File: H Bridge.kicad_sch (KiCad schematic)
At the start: 58 parts, among them J4 Conn_01x02_Socket, Q11 IRLZ44N, Q110 IRLZ44N, Q111 BC557, Q112 BC547, Q113 BC557, Q120 IRLZ44N, Q121 BC557, Q122 BC547, Q123 BC557, Q14 BC547, Q15 BC557, Q17 BC547, Q18 BC547, Q2 BC547, Q210 BC547, Q6 BC547, Q7 BC557, Q9 IRLZ44N, U110 4N35, U2 4N35, U6 4N35, U7 4N35

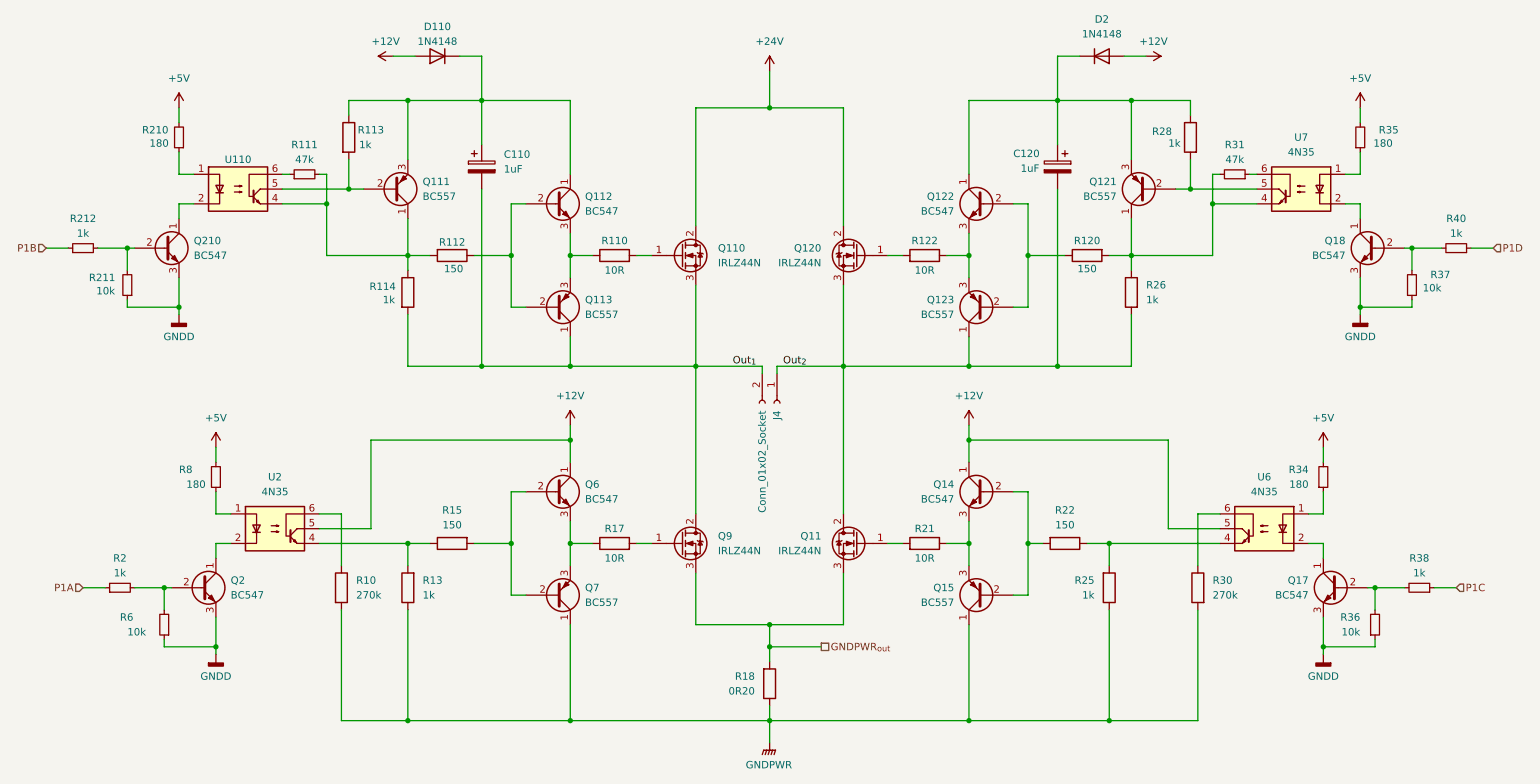
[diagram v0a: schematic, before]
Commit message: Placement H bridge & PSU
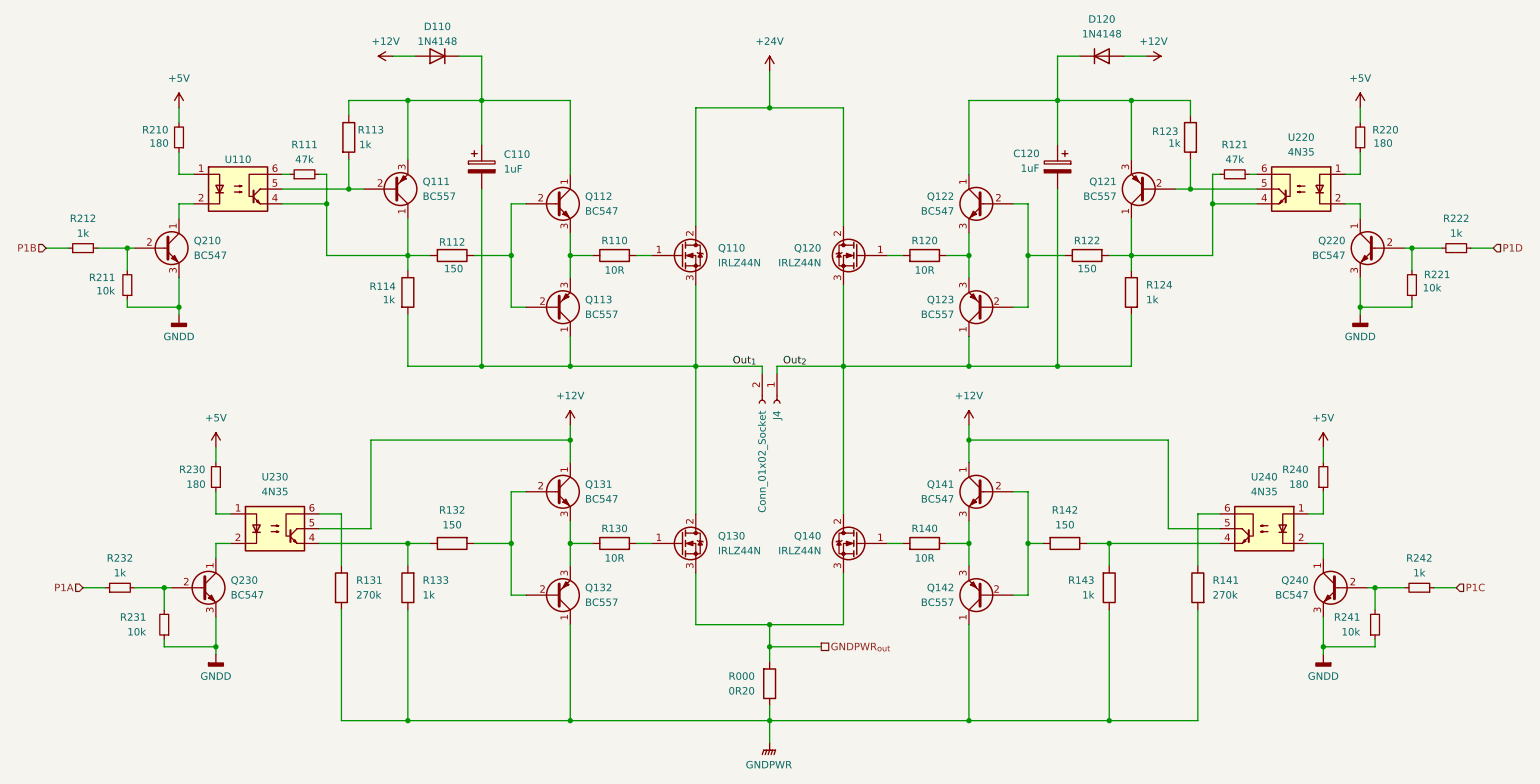
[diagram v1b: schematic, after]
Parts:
- renumbered D2 to D120, Q9 to Q130, Q6 to Q131, Q7 to Q132, Q11 to Q140, Q14 to Q141, Q15 to Q142, Q18 to Q220, Q2 to Q230, Q17 to Q240, R18 to R000, R122 to R120, R31 to R121, R120 to R122, R28 to R123, R26 to R124, R17 to R130, R10 to R131, R15 to R132, R13 to R133, R21 to R140, R30 to R141, R22 to R142, R25 to R143, R35 to R220, R37 to R221, R40 to R222, R8 to R230, R6 to R231, R2 to R232, R34 to R240, R36 to R241, R38 to R242, U7 to U220, U2 to U230, U6 to U240
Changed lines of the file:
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@@
 		(on_board yes)
 		(dnp no)
-		(property "Reference" "R122"
+		(property "Reference" "R120"
 			(at 175.26 64.77 90)
 			(effects
@@
 		(dnp no)
 		(fields_autoplaced yes)
-		(property "Reference" "R36"
+		(property "Reference" "R241"
 			(at 250.19 129.5399 0)
 			(effects
@@
 		(on_board yes)
 		(dnp no)
-		(property "Reference" "R2"
+		(property "Reference" "R232"
 			(at 36.83 119.38 90)
 			(effects
@@
 		(on_board yes)
 		(dnp no)
-		(property "Reference" "Q7"
+		(property "Reference" "Q132"
 			(at 116.84 124.4599 0)
 			(effects
@@
 		(dnp no)
 		(fields_autoplaced yes)
-		(property "Reference" "Q11"
+		(property "Reference" "Q140"
 			(at 157.48 115.5699 0)
 			(effects
@@
 		(dnp no)
 		(fields_autoplaced yes)
-		(property "Reference" "U7"
+		(property "Reference" "U220"
 			(at 240.03 46.99 0)
 			(effects
@@
 		(dnp no)
 		(fields_autoplaced yes)
-		(property "Reference" "R30"
+		(property "Reference" "R141"
 			(at 224.79 123.1899 0)
 			(effects
@@
 		(dnp no)
 		(fields_autoplaced yes)
-		(property "Reference" "Q14"
+		(property "Reference" "Q141"
 			(at 180.34 106.6799 0)
 			(effects
@@
 		(on_board yes)
 		(dnp no)
-		(property "Reference" "R8"
+		(property "Reference" "R230"
 			(at 46.99 104.14 0)
 			(effects
@@
 		(on_board yes)
 		(dnp no)
-		(property "Reference" "U2"
+		(property "Reference" "U230"
 			(at 63.5 105.41 0)
 			(effects
@@
 		(on_board yes)
 		(dnp no)
-		(property "Reference" "Q15"
+		(property "Reference" "Q142"
 			(at 180.34 124.4599 0)
 			(effects
@@
 		(dnp no)
 		(fields_autoplaced yes)
-		(property "Reference" "D2"
+		(property "Reference" "D120"
 			(at 205.74 26.67 0)
 			(effects
@@
 		(on_board yes)
 		(dnp no)
-		(property "Reference" "R6"
+		(property "Reference" "R231"
 			(at 36.83 129.54 0)
 			(effects
@@
 		(dnp no)
 		(fields_autoplaced yes)
-		(property "Reference" "R10"
+		(property "Reference" "R131"
 			(at 77.47 123.1899 0)
 			(effects
@@
 		(on_board yes)
 		(dnp no)
-		(property "Reference" "R34"
+		(property "Reference" "R240"
 			(at 241.3 104.1399 0)
 			(effects
@@
 		(dnp no)
 		(fields_autoplaced yes)
-		(property "Reference" "Q17"
+		(property "Reference" "Q240"
 			(at 241.3 123.1899 0)
 			(effects
@@
 		(dnp no)
 		(fields_autoplaced yes)
-		(property "Reference" "Q9"
+		(property "Reference" "Q130"
 			(at 139.7 115.5699 0)
 			(effects
@@
 		(on_board yes)
 		(dnp no)
-		(property "Reference" "R37"
+		(property "Reference" "R221"
 			(at 265.684 70.612 0)
 			(effects
@@
 		(on_board yes)
 		(dnp no)
-		(property "Reference" "R15"
+		(property "Reference" "R132"
 			(at 93.98 111.125 90)
 			(effects
@@
 		(dnp no)
 		(fields_autoplaced yes)
-		(property "Reference" "R18"
+		(property "Reference" "R000"
 			(at 146.05 139.6999 0)
 			(effects
@@
 			(project "Motor Control"
 				(path "/287fa568-d091-4161-b3b2-3036dfbfe9fa/78ba1051-b673-42a0-97cc-c42edd42c782"
-					(reference "R18")
+					(reference "R000")
 					(unit 1)
 				)
@@
 		(dnp no)
 		(fields_autoplaced yes)
-		(property "Reference" "Q18"
+		(property "Reference" "Q220"
 			(at 247.65 64.7699 0)
 			(effects
@@
 		(on_board yes)
 		(dnp no)
-		(property "Reference" "R35"
+		(property "Reference" "R220"
 			(at 256.794 45.72 0)
 			(effects
@@
 		(dnp no)
 		(fields_autoplaced yes)
-		(property "Reference" "R13"
+		(property "Reference" "R133"
 			(at 88.9 123.1899 0)
 			(effects
@@
 		(dnp no)
 		(fields_autoplaced yes)
-		(property "Reference" "R25"
+		(property "Reference" "R143"
 			(at 204.47 123.1899 0)
 			(effects
@@
 		(on_board yes)
 		(dnp no)
-		(property "Reference" "R26"
+		(property "Reference" "R124"
 			(at 213.36 72.3899 0)
 			(effects
@@
 		(on_board yes)
 		(dnp no)
-		(property "Reference" "R17"
+		(property "Reference" "R130"
 			(at 121.92 114.3 90)
 			(effects
@@
 		(dnp no)
 		(fields_autoplaced yes)
-		(property "Reference" "R38"
+		(property "Reference" "R242"
 			(at 260.35 119.38 90)
 			(effects
@@
 		(on_board yes)
 		(dnp no)
-		(property "Reference" "U6"
+		(property "Reference" "U240"
 			(at 233.68 105.41 0)
 			(effects
@@
 		(on_board yes)
 		(dnp no)
-		(property "Reference" "R28"
+		(property "Reference" "R123"
 			(at 214.376 45.974 0)
 			(effects
@@
 		(on_board yes)
 		(dnp no)
-		(property "Reference" "R22"
+		(property "Reference" "R142"
 			(at 199.39 111.125 90)
 			(effects
@@
 		(dnp no)
 		(fields_autoplaced yes)
-		(property "Reference" "Q6"
+		(property "Reference" "Q131"
 			(at 116.84 106.6799 0)
 			(effects
@@
 		(on_board yes)
 		(dnp no)
-		(property "Reference" "R21"
+		(property "Reference" "R140"
 			(at 175.26 114.3 90)
 			(effects
@@
 		(dnp no)
 		(fields_autoplaced yes)
-		(property "Reference" "Q2"
+		(property "Reference" "Q230"
 			(at 55.88 123.1899 0)
 			(effects
@@
 		(on_board yes)
 		(dnp no)
-		(property "Reference" "R31"
+		(property "Reference" "R121"
 			(at 228.6 48.26 90)
 			(effects
@@
 		(dnp no)
 		(fields_autoplaced yes)
-		(property "Reference" "R40"
+		(property "Reference" "R222"
 			(at 266.7 60.96 90)
 			(effects
@@
 		(on_board yes)
 		(dnp no)
-		(property "Reference" "R120"
+		(property "Reference" "R122"
 			(at 203.2 64.77 90)
 			(effects

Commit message: Update 090725
New footprints added
Schematic made into sub schematics
PCB needs work
Component references need to be sorted for the most part
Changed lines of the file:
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@@
 (kicad_sch
-	(version 20231120)
+	(version 20250114)
 	(generator "eeschema")
-	(generator_version "8.0")
+	(generator_version "9.0")
 	(paper "A4")
 	(title_block
@@
 	(label "Out_{1}"
 		(at 142.24 86.36 0)
-		(fields_autoplaced yes)
 		(effects
 			(font
@@
 	(label "Out_{2}"
 		(at 154.94 86.36 180)
-		(fields_autoplaced yes)
 		(effects
 			(font
@@
 		(shape input)
 		(at 30.48 124.46 180)
-		(fields_autoplaced yes)
 		(effects
 			(font
@@
 		(shape input)
 		(at 273.05 66.04 0)
-		(fields_autoplaced yes)
 		(effects
 			(font
@@
 		(shape input)
 		(at 24.13 66.04 180)
-		(fields_autoplaced yes)
 		(effects
 			(font
@@
 		(shape passive)
 		(at 157.48 134.62 0)
-		(fields_autoplaced yes)
 		(effects
 			(font
@@
 		(shape input)
 		(at 266.7 124.46 0)
-		(fields_autoplaced yes)
 		(effects
 			(font

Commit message: V 1.0 fabrication output
V 1.0 ready for fabrication
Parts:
- Q110, Q120, Q130, Q140: footprint Package_TO_SOT_THT:TO-220-3_Horizontal_TabDown -> User:TO-220-3_Horizontal_TabDown_HoleToCenter
- renumbered U110 to U210
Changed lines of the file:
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@@
 		(title "Motor Control")
 		(date "2025-07-03")
-		(rev "0.1.0")
+		(rev "1.0")
 		(company "AARHUS TECH")
 	)
@@
 			)
 		)
-		(property "Footprint" "Package_TO_SOT_THT:TO-220-3_Horizontal_TabDown"
+		(property "Footprint" "User:TO-220-3_Horizontal_TabDown_HoleToCenter"
 			(at 139.7 69.215 0)
 			(effects
@@
 			)
 		)
-		(property "Footprint" "Package_TO_SOT_THT:TO-220-3_Horizontal_TabDown"
+		(property "Footprint" "User:TO-220-3_Horizontal_TabDown_HoleToCenter"
 			(at 157.48 118.745 0)
 			(effects
@@
 			)
 		)
-		(property "Footprint" "Package_TO_SOT_THT:TO-220-3_Horizontal_TabDown"
+		(property "Footprint" "User:TO-220-3_Horizontal_TabDown_HoleToCenter"
 			(at 158.75 69.215 0)
 			(effects
@@
 			)
 		)
-		(property "Footprint" "Package_TO_SOT_THT:TO-220-3_Horizontal_TabDown"
+		(property "Footprint" "User:TO-220-3_Horizontal_TabDown_HoleToCenter"
 			(at 139.7 118.745 0)
 			(effects
@@
 		(on_board yes)
 		(dnp no)
-		(property "Reference" "U110"
+		(property "Reference" "U210"
 			(at 57.15 50.8 0)
 			(effects
@@
 			(project "Motor Control"
 				(path "/287fa568-d091-4161-b3b2-3036dfbfe9fa/78ba1051-b673-42a0-97cc-c42edd42c782"
-					(reference "U110")
+					(reference "U210")
 					(unit 1)
 				)

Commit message: Partnumbers
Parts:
- U210, U220, U230, U240: Part number (none) -> 1021351; Supplier (none) -> Farnell

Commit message: BOM
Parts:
- C110, C120: value 1uF -> 2.2uF; Part number (none) -> 8766797; Supplier (none) -> Farnell
- D110, D120: Part number (none) -> 00.001.4148; Supplier (none) -> Cypax
- Q110, Q120, Q130, Q140: Part number (none) -> 8651418; Supplier (none) -> Farnell
- Q111, Q113, Q121, Q123, Q132, Q142: Part number (none) -> 01.020.0557; Supplier (none) -> Cypax
- Q112, Q122, Q131, Q141, Q210, Q220, Q230, Q240: Part number (none) -> 01.020.0547; Supplier (none) -> Cypax
- R000: Part number (none) -> 846-9836; Supplier (none) -> RS
- R110, R120, R130, R140: Part number (none) -> 05.000.0210; Supplier (none) -> Cypax
- R111, R121: Part number (none) -> 05.000.0547; Supplier (none) -> Cypax
- R112, R122, R132, R142: Part number (none) -> 05.000.0315; Supplier (none) -> Cypax
- R113, R114, R123, R124, R133, R143, R212, R222, R232, R242: Part number (none) -> 05.000.0410; Supplier (none) -> Cypax
- R131, R141: Part number (none) -> 05.000.0627; Supplier (none) -> Cypax
- R210, R220, R230, R240: Part number (none) -> 05.000.0318; Supplier (none) -> Cypax
- R211, R221, R231, R241: Part number (none) -> 05.000.0510; Supplier (none) -> Cypax
